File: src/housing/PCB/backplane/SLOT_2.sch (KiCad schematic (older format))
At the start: 1 part, among them J1 10018784-10201TLF

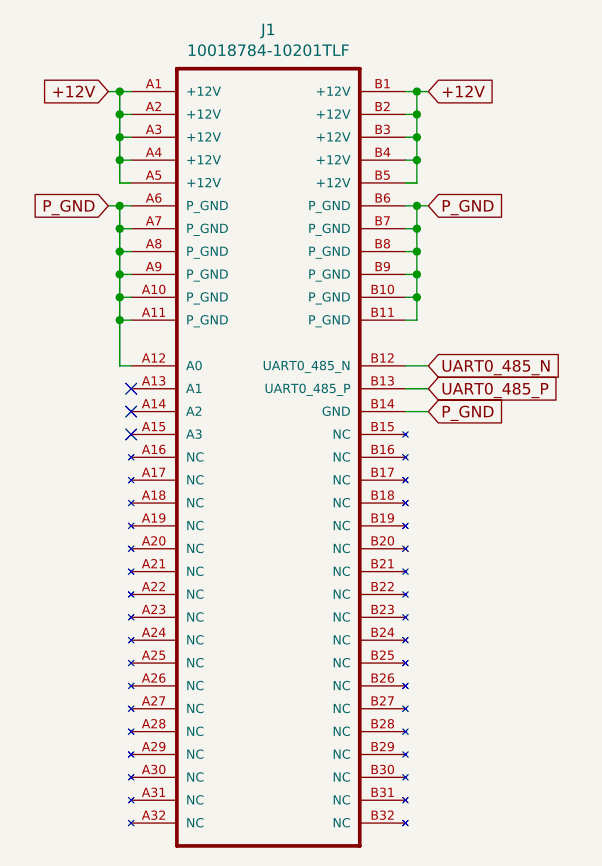
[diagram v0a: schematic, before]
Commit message: fixing backplane libraries path error
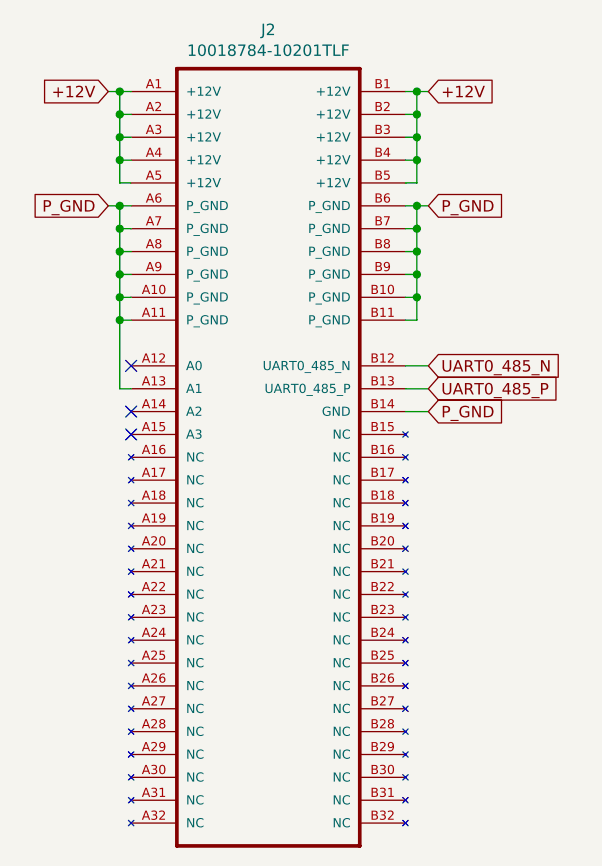
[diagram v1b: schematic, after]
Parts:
- removed J1: 10018784-10201TLF, kicad-lib:CONN_10018784-10201TLF, symbol 10018784-10201TLF:10018784-10201TLF
- added J2: 10018784-10201TLF, kicad-lib:CONN_10018784-10201TLF, symbol 10018784-10201TLF:10018784-10201TLF
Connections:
- net +12V: now also J2.A1 (+12V), J2.A2 (+12V), J2.A3 (+12V), J2.A4 (+12V), J2.A5 (+12V), J2.B1 (+12V), J2.B2 (+12V), J2.B3 (+12V), J2.B4 (+12V), J2.B5 (+12V)
- net P_GND: now also J2.A10 (P_GND), J2.A11 (P_GND), J2.A13 (A1), J2.A6 (P_GND), J2.A7 (P_GND), J2.A8 (P_GND), J2.A9 (P_GND), J2.B10 (P_GND), J2.B11 (P_GND), J2.B14 (GND), J2.B6 (P_GND), J2.B7 (P_GND), J2.B8 (P_GND), J2.B9 (P_GND)
- net UART0_485_N: now also J2.B12 (UART0_485_N)
- net UART0_485_P: now also J2.B13 (UART0_485_P)
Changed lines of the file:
@@
 $Descr A4 11693 8268
 encoding utf-8
-Sheet 2 9
-Title ""
+Sheet 3 9
+Title "ACS backplane"
 Date ""
-Rev ""
-Comp ""
-Comment1 ""
+Rev "1"
+Comp "Halidelabs"
+Comment1 "contact@halidelabs.eu"
 Comment2 ""
 Comment3 ""
@@
 $EndDescr
 $Comp
-L 10018784-10201TLF:10018784-10201TLF J1
-U 1 1 5DF19CC0
+L 10018784-10201TLF:10018784-10201TLF J?
+U 1 1 5DF52F10
 P 5600 3950
-AR Path="/5DF19C0C/5DF19CC0" Ref="J1"  Part="1"
-AR Path="/5DF2A71E/5DF19CC0" Ref="J?"  Part="1"
-AR Path="/5DF2E10A/5DF19CC0" Ref="J?"  Part="1"
-AR Path="/5DF2E1F6/5DF19CC0" Ref="J?"  Part="1"
-AR Path="/5DF2E246/5DF19CC0" Ref="J?"  Part="1"
-AR Path="/5DF2E24A/5DF19CC0" Ref="J?"  Part="1"
-F 0 "J1" H 5600 5820 50  0000 C CNN
+AR Path="/5DF19C0C/5DF52F10" Ref="J?"  Part="1"
+AR Path="/5DF2A71E/5DF52F10" Ref="J?"  Part="1"
+AR Path="/5DF2E10A/5DF52F10" Ref="J2"  Part="1"
+AR Path="/5DF2E1F8/5DF52F10" Ref="J?"  Part="1"
+AR Path="/5DF2E248/5DF52F10" Ref="J?"  Part="1"
+AR Path="/5DF2E24C/5DF52F10" Ref="J?"  Part="1"
+F 0 "J2" H 5600 5820 50  0000 C CNN
 F 1 "10018784-10201TLF" H 5600 5729 50  0000 C CNN
 F 2 "kicad-lib:CONN_10018784-10201TLF" H 5650 4450 50  0001 L BNN
@@
 Wire Wire Line
 	6300 3750 6200 3750
+Connection ~ 4950 3350
 Wire Wire Line
-	4950 3350 4950 3550
+	4950 3650 5000 3650
 Wire Wire Line
-	4950 3550 5000 3550
-Connection ~ 4950 3350
-NoConn ~ 5000 3650
+	4950 3350 4950 3650
+NoConn ~ 5000 3550
 NoConn ~ 5000 3750
 NoConn ~ 5000 3850
